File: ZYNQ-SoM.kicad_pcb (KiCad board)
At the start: 6 copper layers, 50 x 40 mm, 173 parts, among them IC501 TPS51206DSQR, J401 AXK500137YG, J402 AXK500137YG, Q201 MMBT3904, U201 xc7z010clg400, U202 W25Q256FVEI, U301 MT41K256M16TW-107_P, U501 TPS62130ARGTR, U502 TPS62130ARGTR, U503 SPX3819M5-L-3-3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

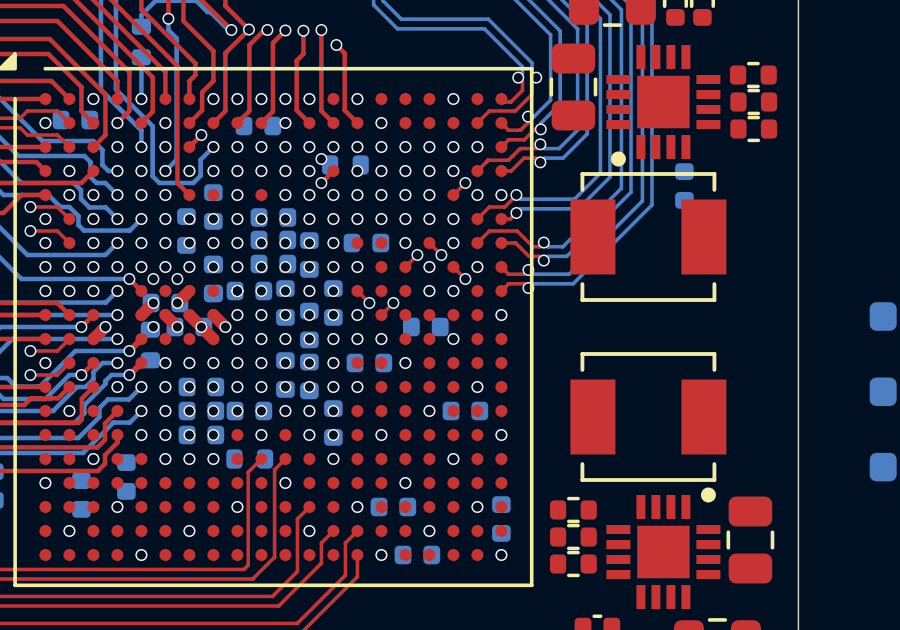
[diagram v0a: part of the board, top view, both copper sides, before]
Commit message: layout: continue layout pl io
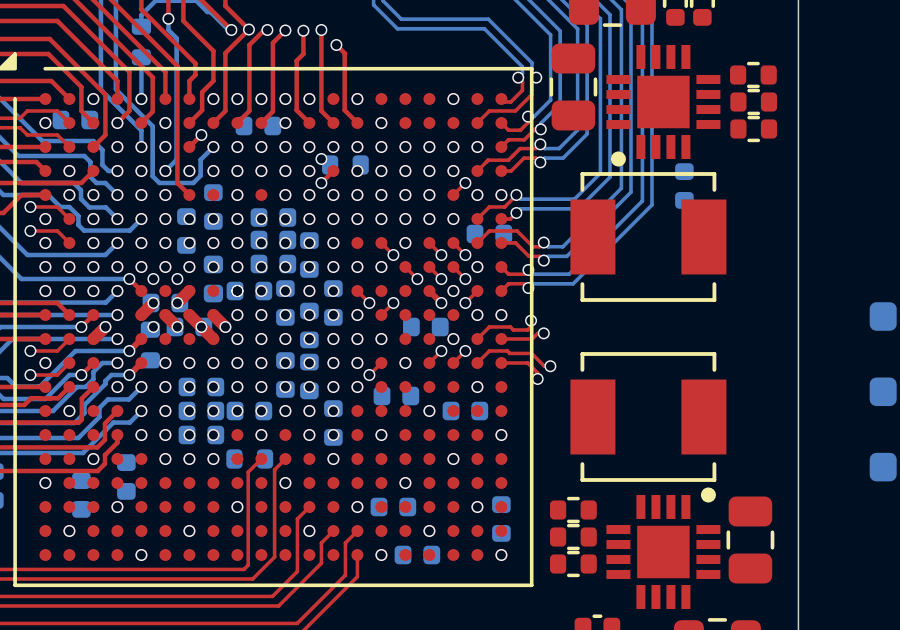
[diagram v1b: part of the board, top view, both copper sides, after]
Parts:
- moved C571 4.11 mm to (139.7, 76.9)
- moved C555 1.42 mm to (136.6, 82.3)
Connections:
- J402 pad 12: unconnected-(J402-Pad12) -> PL_B35_IO22_P
- J402 pad 14: unconnected-(J402-Pad14) -> PL_B35_IO22_N
- J402 pad 18: unconnected-(J402-Pad18) -> PL_B35_IO20_P
- J402 pad 20: unconnected-(J402-Pad20) -> PL_B35_IO20_N
- J402 pad 24: unconnected-(J402-Pad24) -> PL_B35_IO13_P
- J402 pad 26: unconnected-(J402-Pad26) -> PL_B35_IO13_N
- J402 pad 29: unconnected-(J402-Pad29) -> PL_B35_IO19_P
- J402 pad 30: unconnected-(J402-Pad30) -> PL_B35_IO14_P
- J402 pad 31: unconnected-(J402-Pad31) -> PL_B35_IO19_N
- J402 pad 32: unconnected-(J402-Pad32) -> PL_B35_IO14_N
- J402 pad 36: unconnected-(J402-Pad36) -> PL_B35_IO16_N
- J402 pad 38: unconnected-(J402-Pad38) -> PL_B35_IO16_P
- J402 pad 42: unconnected-(J402-Pad42) -> PL_B35_IO5_N
- J402 pad 44: unconnected-(J402-Pad44) -> PL_B35_IO5_P
- J402 pad 48: unconnected-(J402-Pad48) -> PL_B35_IO23_N
- J402 pad 50: unconnected-(J402-Pad50) -> PL_B35_IO23_P
- J402 pad 54: unconnected-(J402-Pad54) -> PL_B35_IO7_N
- J402 pad 56: unconnected-(J402-Pad56) -> PL_B35_IO7_P
- J402 pad 60: unconnected-(J402-Pad60) -> PL_B35_IO8_P
- J402 pad 62: unconnected-(J402-Pad62) -> PL_B35_IO8_N
- J402 pad 66: unconnected-(J402-Pad66) -> PL_B35_IO9_N
- J402 pad 68: unconnected-(J402-Pad68) -> PL_B35_IO9_P
- J402 pad 72: unconnected-(J402-Pad72) -> PL_B35_IO10_P
- J402 pad 74: unconnected-(J402-Pad74) -> PL_B35_IO10_N
- J402 pad 78: unconnected-(J402-Pad78) -> PL_B35_IO3_N
- J402 pad 80: unconnected-(J402-Pad80) -> PL_B35_IO3_P
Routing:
- net PL_B35_IO23_N: track 0.00 -> 54.1 mm, vias 0 -> 2
- net PL_B35_IO23_P: track 0.00 -> 53.2 mm, vias 0 -> 2
- net PL_B35_IO7_P: track 0.00 -> 45.5 mm, vias 0 -> 2
- net PL_B35_IO8_P: track 0.00 -> 45.4 mm, vias 0 -> 2
- net PL_B35_IO7_N: track 0.00 -> 45.0 mm, vias 0 -> 2
- net PL_B35_IO8_N: track 0.00 -> 44.3 mm, vias 0 -> 2
- net PL_B35_IO9_P: track 0.00 -> 41.7 mm, vias 0 -> 2
- net PL_B35_IO10_N: track 0.00 -> 41.2 mm, vias 0 -> 2
- net PL_B35_IO9_N: track 0.00 -> 41.2 mm, vias 0 -> 2
- net PL_B35_IO10_P: track 0.00 -> 40.9 mm, vias 0 -> 2
- net unconnected-(J402-Pad48): track 37.7 -> 0.00 mm, vias 1 -> 0
- net unconnected-(J402-Pad50): track 37.7 -> 0.00 mm, vias 1 -> 0
- net PL_B35_IO22_P: track 8.29 -> 45.5 mm, vias 1 -> 2
- net PL_B35_IO22_N: track 7.50 -> 44.4 mm, vias 1 -> 2
- net unconnected-(J402-Pad74): track 36.2 -> 0.00 mm, vias 1 -> 0
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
